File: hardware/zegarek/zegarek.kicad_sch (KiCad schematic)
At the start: 0 parts

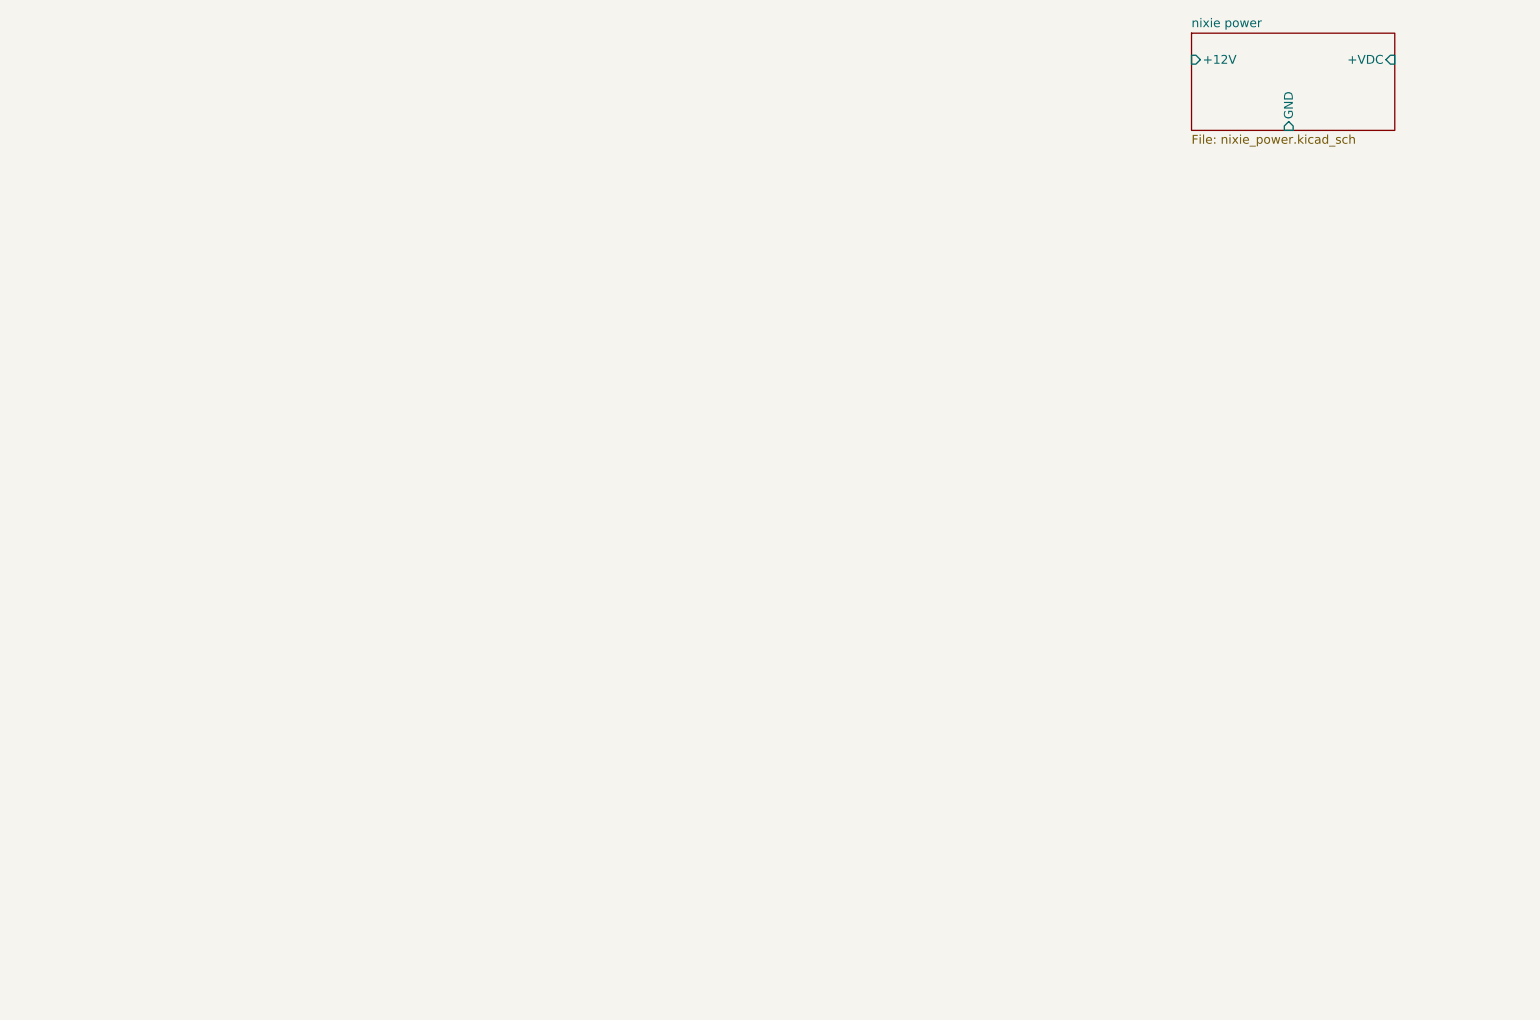
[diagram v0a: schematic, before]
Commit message: page MCU and NIXIE done, nixiepwr changed name to PWR MNG
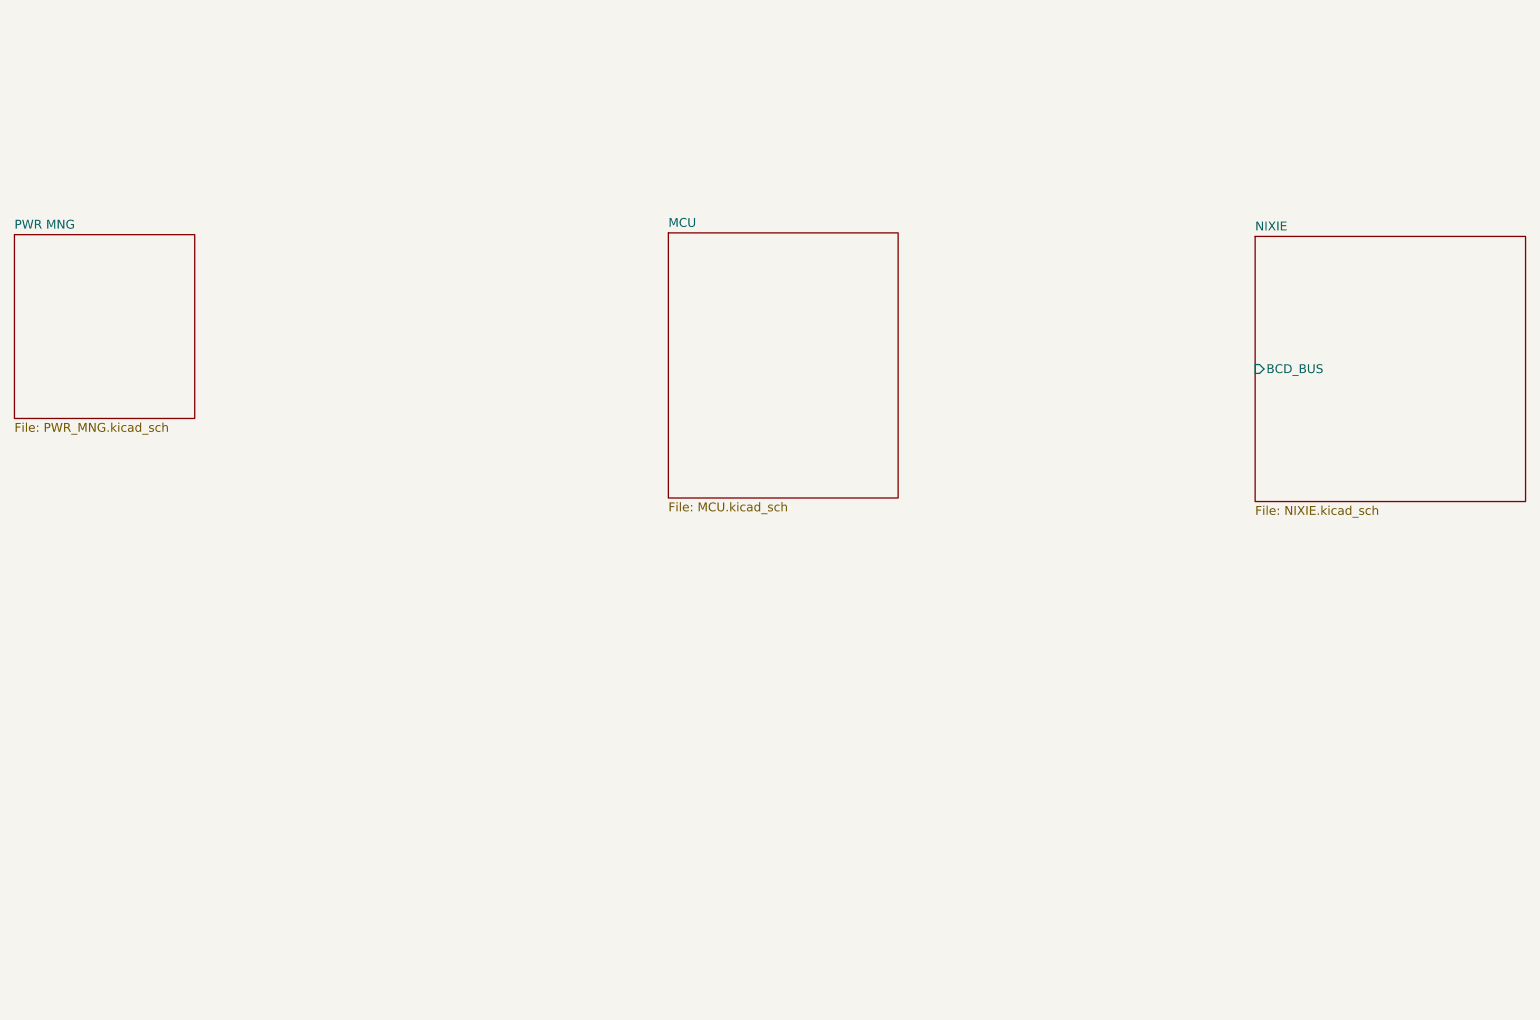
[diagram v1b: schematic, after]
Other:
- sheet nixie power renamed PWR MNG
- added sheet MCU (MCU.kicad_sch)
- added sheet NIXIE (NIXIE.kicad_sch)
- sheet PWR MNG: file nixie_power.kicad_sch -> PWR_MNG.kicad_sch
- sheet PWR MNG ports: added none; removed +12V, +VDC, GND
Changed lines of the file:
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@@
 (kicad_sch
-	(version 20231120)
+	(version 20260306)
 	(generator "eeschema")
-	(generator_version "8.0")
+	(generator_version "10.0")
 	(paper "A4")
 	(sheet
-		(at 194.31 21.59)
-		(size 29.21 13.97)
+		(at 119.126 50.292)
+		(size 33.02 38.1)
+		(exclude_from_sim no)
+		(in_bom yes)
+		(on_board yes)
+		(dnp no)
 		(fields_autoplaced yes)
 		(stroke
@@
 		)
 		(fill
-			(color 0 0 0 0.0000)
+			(color 0 0 0 0)
 		)
-		(property "Sheetname" "nixie power"
-			(at 194.31 20.8784 0)
+		(property "Sheetname" "MCU"
+			(at 119.126 49.5804 0)
+			(show_name no)
+			(do_not_autoplace no)
 			(effects
 				(font
@@
 			)
 		)
-		(property "Sheetfile" "nixie_power.kicad_sch"
-			(at 194.31 36.1446 0)
+		(property "Sheetfile" "MCU.kicad_sch"
+			(at 119.126 88.9766 0)
+			(show_name no)
+			(do_not_autoplace no)
 			(effects
 				(font
@@
 			)
 		)
-		(pin "+12V" input
-			(at 194.31 25.4 180)
+		(instances
+			(project "zegarek"
+				(path "/f4008fb9-ad6b-45c6-9bc0-571e7640a726"
+					(page "3")
+				)
+			)
+		)
+	)
+	(sheet
+		(at 203.454 50.8)
+		(size 38.862 38.1)
+		(exclude_from_sim no)
+		(in_bom yes)
+		(on_board yes)
+		(dnp no)
+		(fields_autoplaced yes)
+		(stroke
+			(width 0.1524)
+			(type solid)
+		)
+		(fill
+			(color 0 0 0 0)
+		)
+		(property "Sheetname" "NIXIE"
+			(at 203.454 50.0884 0)
+			(show_name no)
+			(do_not_autoplace no)
+			(effects
+				(font
+					(size 1.27 1.27)
+				)
+				(justify left bottom)
+			)
+		)
+		(property "Sheetfile" "NIXIE.kicad_sch"
+			(at 203.454 89.4846 0)
+			(show_name no)
+			(do_not_autoplace no)
+			(effects
+				(font
+					(size 1.27 1.27)
+				)
+				(justify left top)
+			)
+		)
+		(pin "BCD_BUS" input
+			(at 203.454 69.85 180)
 			(effects
 				(font
@@
 			)
 		)
-		(pin "GND" input
-			(at 208.28 35.56 270)
+		(instances
+			(project "zegarek"
+				(path "/f4008fb9-ad6b-45c6-9bc0-571e7640a726"
+					(page "4")
+				)
+			)
+		)
+	)
+	(sheet
+		(at 25.146 50.546)
+		(size 25.908 26.416)
+		(exclude_from_sim no)
+		(in_bom yes)
+		(on_board yes)
+		(dnp no)
+		(fields_autoplaced yes)
+		(stroke
+			(width 0.1524)
+			(type solid)
+		)
+		(fill
+			(color 0 0 0 0)
+		)
+		(property "Sheetname" "PWR MNG"
+			(at 25.146 49.8344 0)
+			(show_name no)
+			(do_not_autoplace no)
 			(effects
 				(font
 					(size 1.27 1.27)
 				)
-				(justify left)
+				(justify left bottom)
 			)
 		)
-		(pin "+VDC" input
-			(at 223.52 25.4 0)
+		(property "Sheetfile" "PWR_MNG.kicad_sch"
+			(at 25.146 77.5466 0)
+			(show_name no)
+			(do_not_autoplace no)
 			(effects
 				(font
 					(size 1.27 1.27)
 				)
-				(justify right)
+				(justify left top)
 			)
 		)
@@
 		)
 	)
+	(embedded_fonts no)
 )

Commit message: pwr page done
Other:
- sheet MCU ports: added BDC_BUS, BTNDN, BTNOK, BTNUP, BUZZER; removed none
- note added: "12V -> 5V 12V -> 3V3 12V -> 100V"
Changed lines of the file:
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@@
 	(generator_version "10.0")
 	(paper "A4")
+	(text "12V -> 5V\n12V -> 3V3\n12V -> 100V"
+		(exclude_from_sim no)
+		(at 59.182 67.818 0)
+		(effects
+			(font
+				(size 1.27 1.27)
+			)
+		)
+	)
+	(bus
+		(pts
+			(xy 152.4 60.96) (xy 203.2 60.96)
+		)
+		(stroke
+			(width 0)
+			(type default)
+		)
+	)
 	(sheet
-		(at 119.126 50.292)
-		(size 33.02 38.1)
+		(at 119.126 50.8)
+		(size 33.274 37.846)
 		(exclude_from_sim no)
 		(in_bom yes)
@@
 		)
 		(property "Sheetname" "MCU"
-			(at 119.126 49.5804 0)
+			(at 119.126 50.0884 0)
 			(show_name no)
 			(do_not_autoplace no)
@@
 		)
 		(property "Sheetfile" "MCU.kicad_sch"
-			(at 119.126 88.9766 0)
+			(at 119.126 89.2306 0)
 			(show_name no)
 			(do_not_autoplace no)
@@
 				)
 				(justify left top)
+			)
+		)
+		(pin "BDC_BUS" output
+			(at 152.4 60.96 0)
+			(effects
+				(font
+					(size 1.27 1.27)
+				)
+				(justify right)
+			)
+		)
+		(pin "BTNDN" input
+			(at 152.4 85.09 0)
+			(effects
+				(font
+					(size 1.27 1.27)
+				)
+				(justify right)
+			)
+		)
+		(pin "BTNOK" input
+			(at 152.4 80.01 0)
+			(effects
+				(font
+					(size 1.27 1.27)
+				)
+				(justify right)
+			)
+		)
+		(pin "BTNUP" input
+			(at 152.4 82.55 0)
+			(effects
+				(font
+					(size 1.27 1.27)
+				)
+				(justify right)
+			)
+		)
+		(pin "BUZZER" input
+			(at 119.126 85.09 180)
+			(effects
+				(font
+					(size 1.27 1.27)
+				)
+				(justify left)
 			)
 		)
@@
 	)
 	(sheet
-		(at 203.454 50.8)
-		(size 38.862 38.1)
+		(at 203.2 50.8)
+		(size 39.116 38.1)
 		(exclude_from_sim no)
 		(in_bom yes)
@@
 		)
 		(property "Sheetname" "NIXIE"
-			(at 203.454 50.0884 0)
+			(at 203.2 50.0884 0)
 			(show_name no)
 			(do_not_autoplace no)
@@
 		)
 		(property "Sheetfile" "NIXIE.kicad_sch"
-			(at 203.454 89.4846 0)
+			(at 203.2 89.4846 0)
 			(show_name no)
 			(do_not_autoplace no)
@@
 		)
 		(pin "BCD_BUS" input
-			(at 203.454 69.85 180)
+			(at 203.2 60.96 180)
 			(effects
 				(font
@@
 	)
 	(sheet
-		(at 25.146 50.546)
-		(size 25.908 26.416)
+		(at 40.64 50.8)
+		(size 40.894 37.084)
 		(exclude_from_sim no)
 		(in_bom yes)
@@
 		)
 		(property "Sheetname" "PWR MNG"
-			(at 25.146 49.8344 0)
+			(at 40.64 50.0884 0)
 			(show_name no)
 			(do_not_autoplace no)
@@
 		)
 		(property "Sheetfile" "PWR_MNG.kicad_sch"
-			(at 25.146 77.5466 0)
+			(at 40.64 88.4686 0)
 			(show_name no)
 			(do_not_autoplace no)

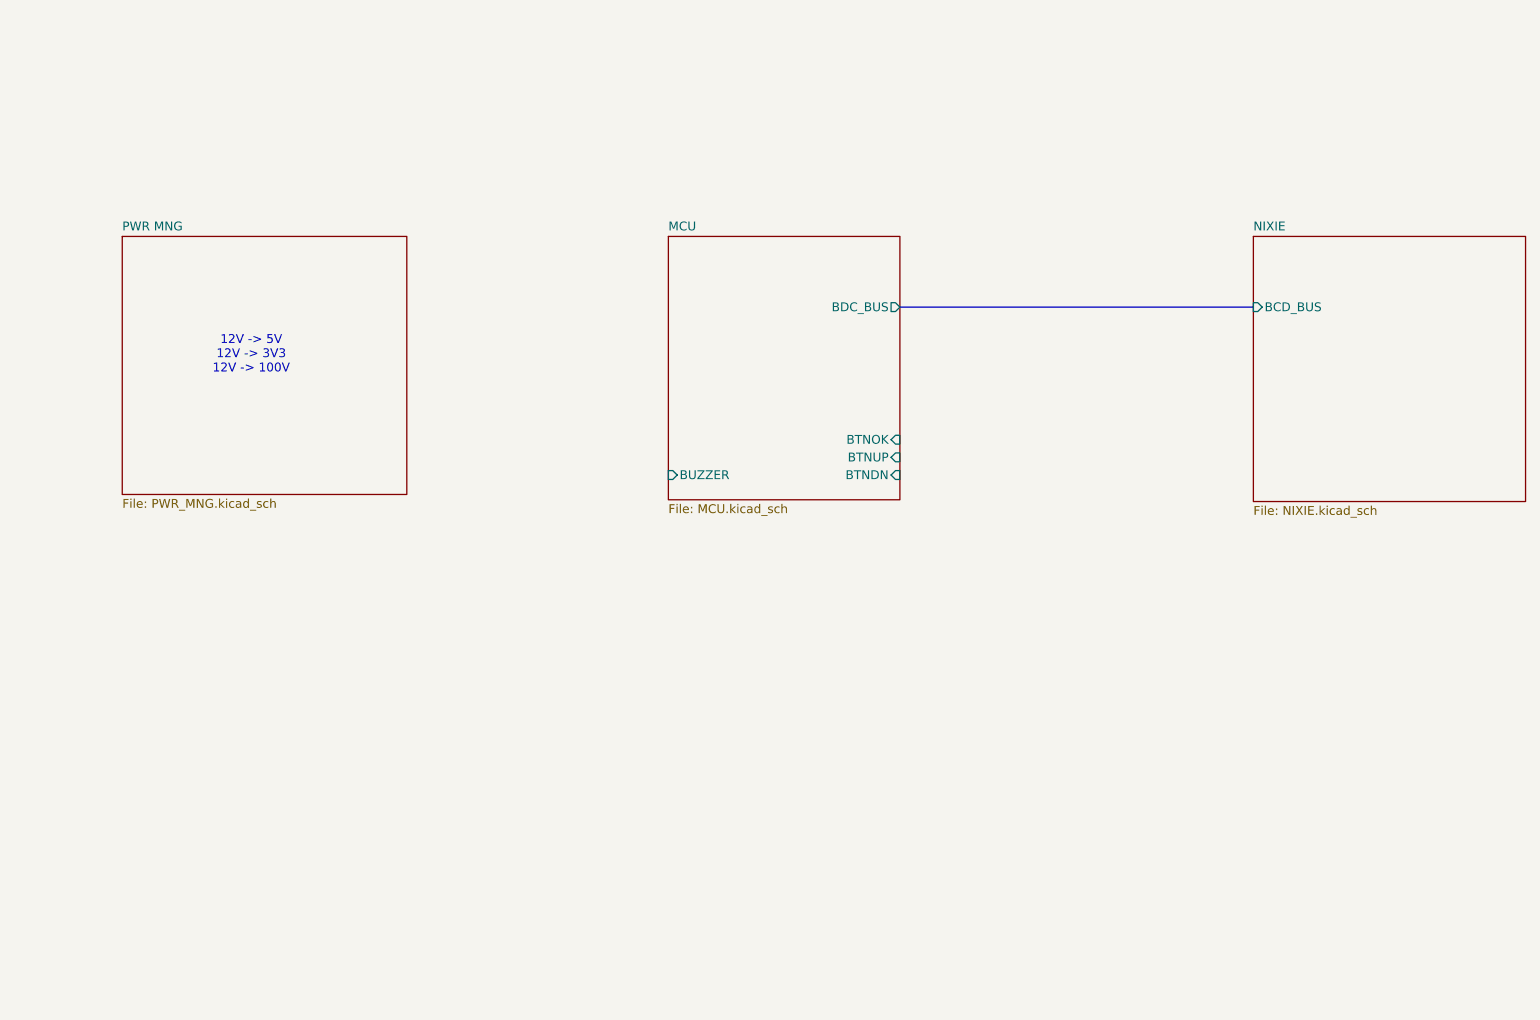
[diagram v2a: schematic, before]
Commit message: added status leds buttons and buzzer, 100V header deleted, footprints assigned
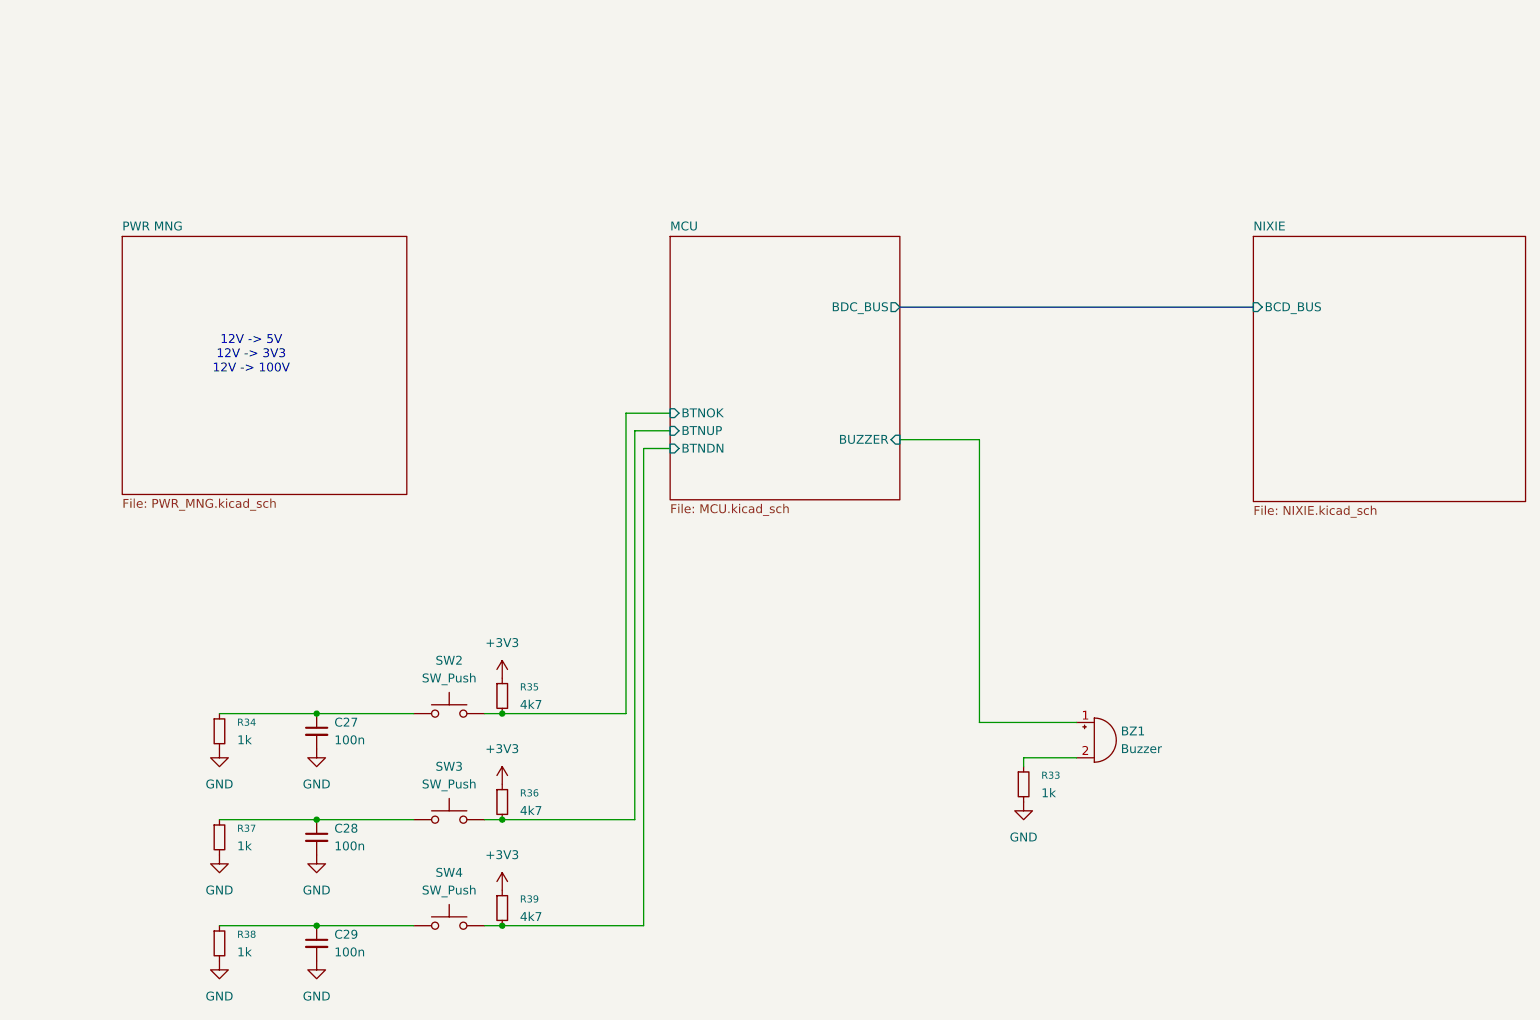
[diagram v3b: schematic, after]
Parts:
- added BZ1: Buzzer, Buzzer_Beeper:MagneticBuzzer_StarMicronics_HMB, symbol Device:Buzzer
- added C27, C28, C29: 100n, Capacitor_SMD:C_1206_3216Metric_Pad1.33x1.80mm_HandSolder, symbol Device:C_Small
- added R33, R34, R37, R38: 1k, Resistor_SMD:R_0201_0603Metric_Pad0.64x0.40mm_HandSolder, symbol Device:R_Small
- added R35, R36, R39: 4k7, Resistor_SMD:R_0201_0603Metric_Pad0.64x0.40mm_HandSolder, symbol Device:R_Small
- added SW2, SW3, SW4: SW_Push, Button_Switch_SMD:SW_Push_1P1T_NO_CK_KMR2, symbol Switch:SW_Push
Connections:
- net MCU/BTNDN: now also R39.2, SW4.2
- net MCU/BTNOK: now also R35.2, SW2.2
- net MCU/BTNUP: now also R36.2, SW3.2
- net MCU/BUZZER: now also BZ1.1 (+)
- new net: BZ1.2 (-), R33.1
- new net: C28.1, R37.1, SW3.1
- new net: C27.1, R34.1, SW2.1
- new net: C29.1, R38.1, SW4.1
- new net +3V3: R35.1, R36.1, R39.1
- new net GND: C27.2, C28.2, C29.2, R33.2, R34.2, R37.2, R38.2
